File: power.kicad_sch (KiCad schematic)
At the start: 40 parts, among them T1 net-tie, U2 TPS546D24ARVFR

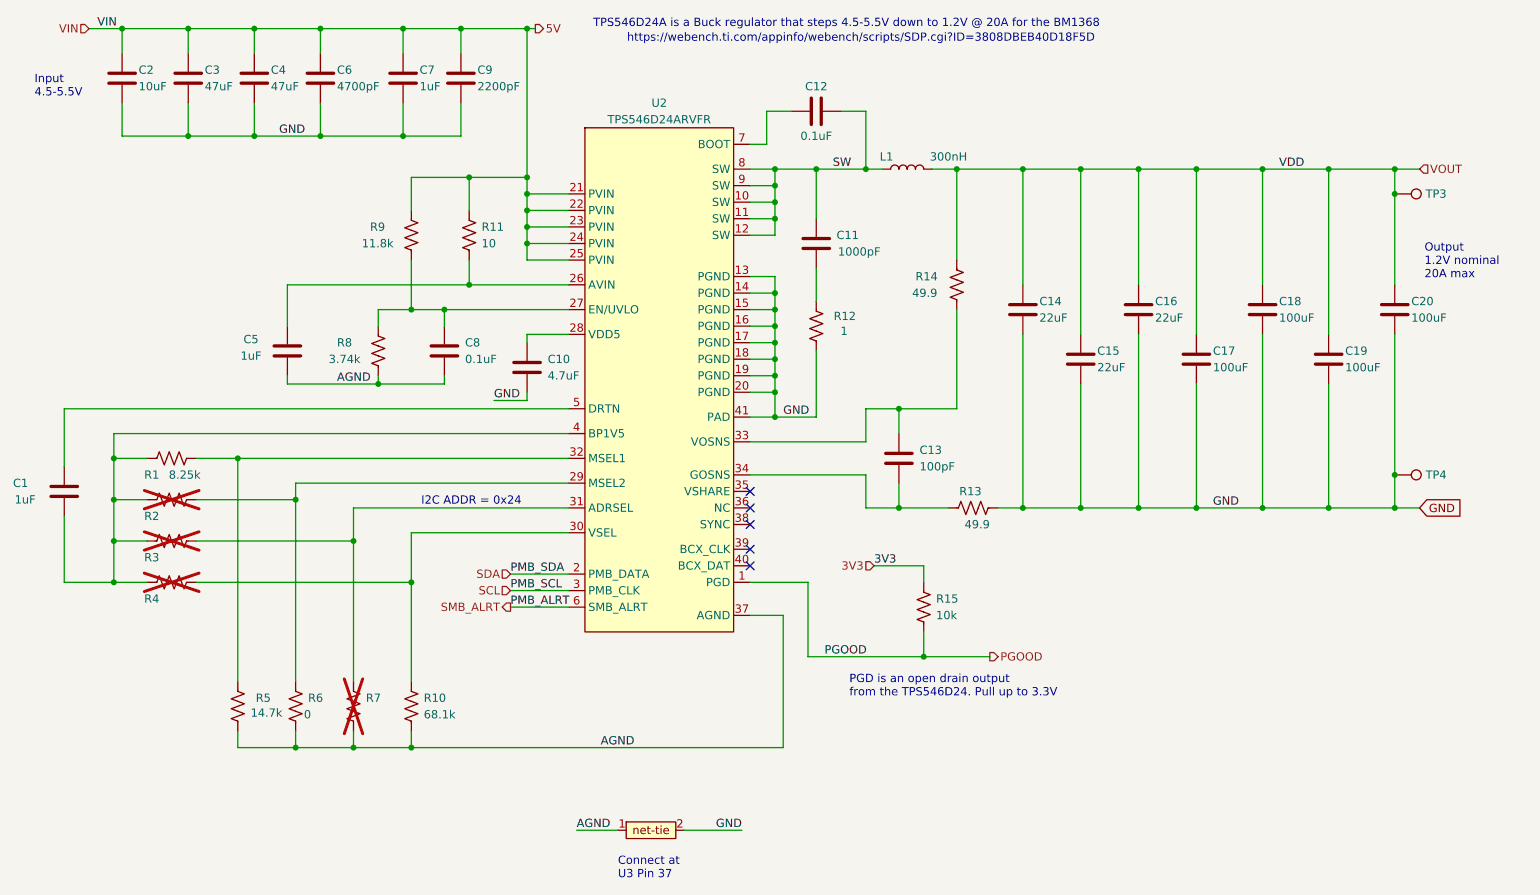
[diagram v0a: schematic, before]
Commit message: eco-603-impl: schematic ECO (E0-E6, R2-R3)
E0 #6/8bd74c8: R21 removed, U9.8 to 1V2, U9.9 direct GND.
E1 #47: U2 SYNC/BCX_CLK/BCX_DAT to AGND.
E2 #25 + R2: R30-R32 4k7 PMBus, R35 10k PGD pull-ups.
E3 #13/#16: R22/R23 100R to 10R.
E4 #11/#17: F1 5A series, D1 SMAJ5.0A, C60 bulk.
E5 #37 + R3: R33/R34 5k1 CC, D2/D5 USB ESD, D3/D4 I2C ESD.
R3: C61 47u + C62 100n PVIN/AVIN bulk.
Rev 601->603. ERC: 18->19 err (PVIN PWR flag side effect of F1,
same benign class); netlist-verified, geometry-audited.
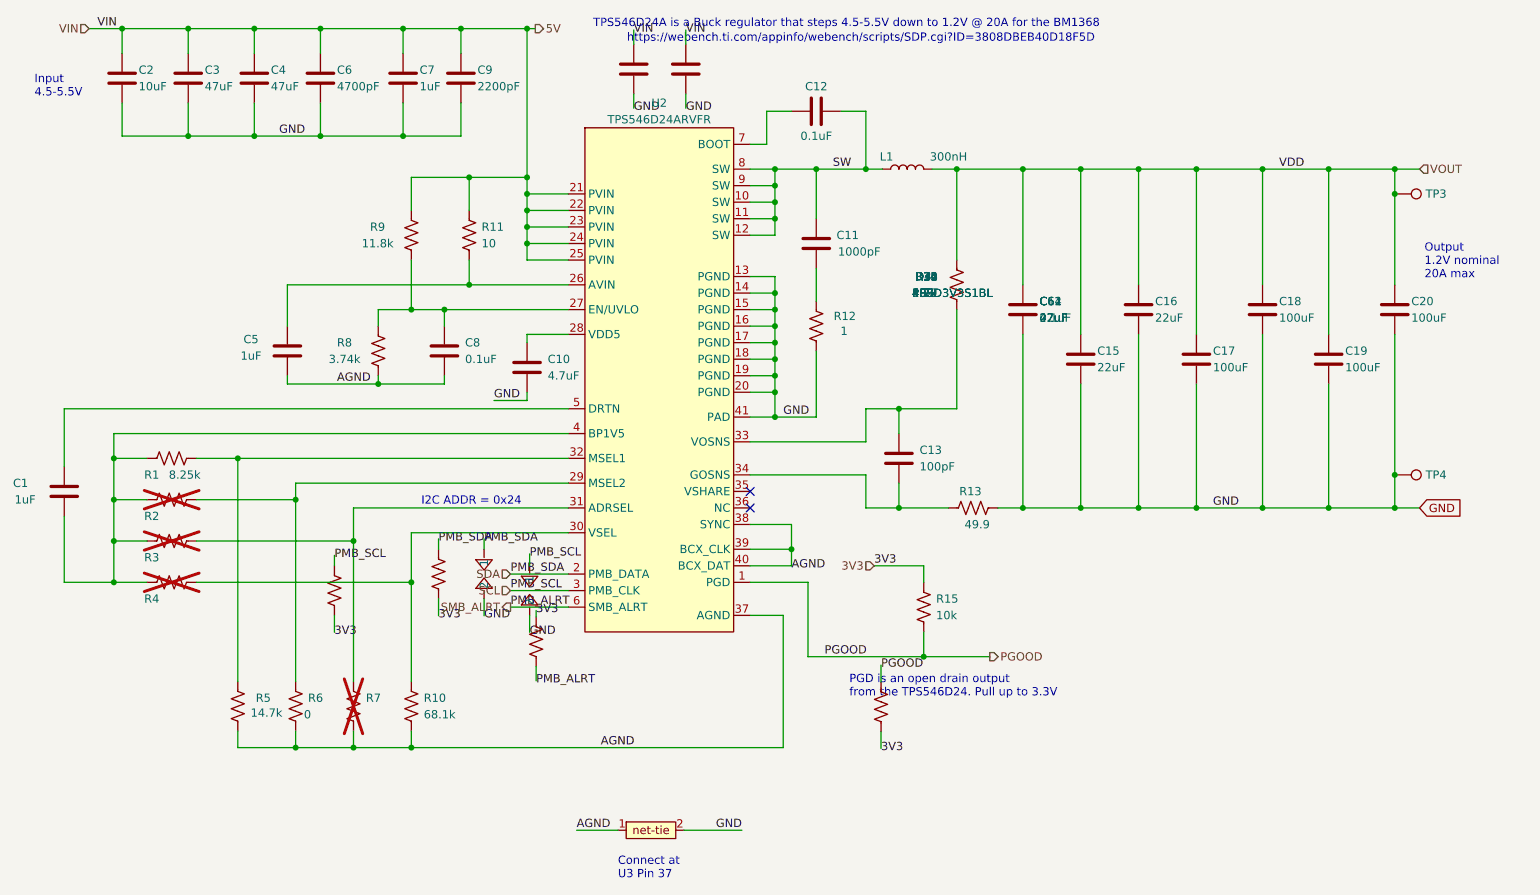
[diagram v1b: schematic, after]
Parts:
- added C61: 47uF, Capacitor_SMD:C_1206_3216Metric, symbol Device:C
- added C62: 0.1uF, Capacitor_SMD:C_0402_1005Metric, symbol Device:C
- added D3, D4: PESD3V3S1BL, Diode_SMD:D_SOD-323, symbol bitaxe:TVS_BIDIR
- added R30, R31, R32: 4.7k, Resistor_SMD:R_0402_1005Metric, symbol Device:R_US
- added R35: 10k, Resistor_SMD:R_0402_1005Metric, symbol Device:R_US
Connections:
- net 3V3: now also R30.2, R31.2, R32.1, R35.2
- net 5V: now also C61.1, C62.1
- net AGND: now also U2.38 (SYNC), U2.39 (BCX_CLK), U2.40 (BCX_DAT)
- net GND: now also C61.2, C62.2, D3.2, D4.2
- net PGOOD: now also R35.1
- net SCL: now also D4.1, R31.1
- net SDA: now also D3.1, R30.1
- net SMB_ALRT: now also R32.2
- no-connect marks 5 -> 2

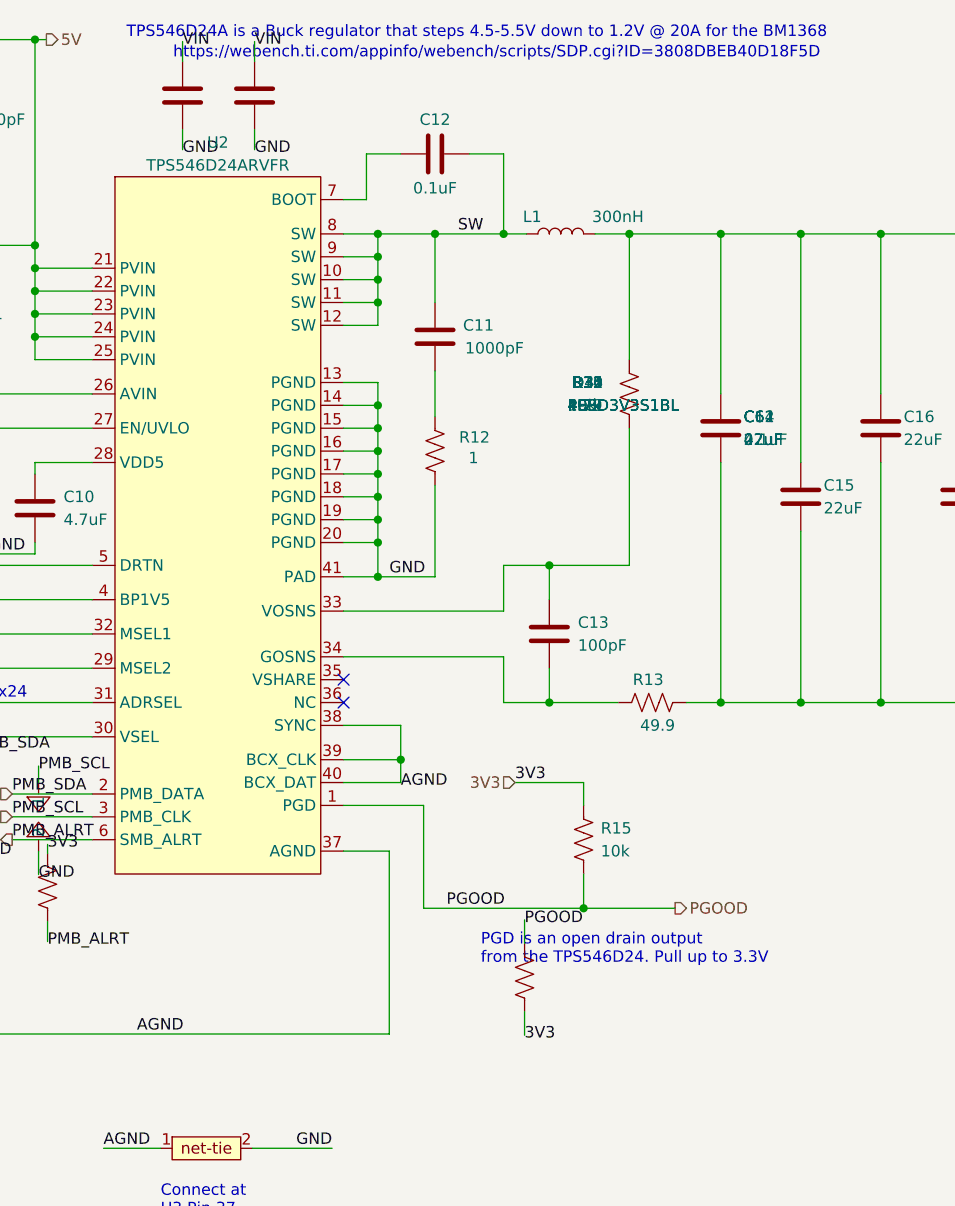
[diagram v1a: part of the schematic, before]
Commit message: eco-603-impl: PCB re-layout rev 603 (DRC 0 new) + manufacturing
PCB impl v7 (impl_pcb_603.py): herencia 602 + fixes E1-E6/R2-R3.
DRC con refill: 5 violaciones = base preexistente, 0 nuevas,
0 unconnected (drc_newZ.txt).
Regenera Gerbers/.drl/BOM/PDF esquematico desde esquematicos ECO
(sin R35/C61, D2->D2+D5, C60 1210, C62). iBOM html sin cambios
(no regenerable con kicad-cli; anotado).
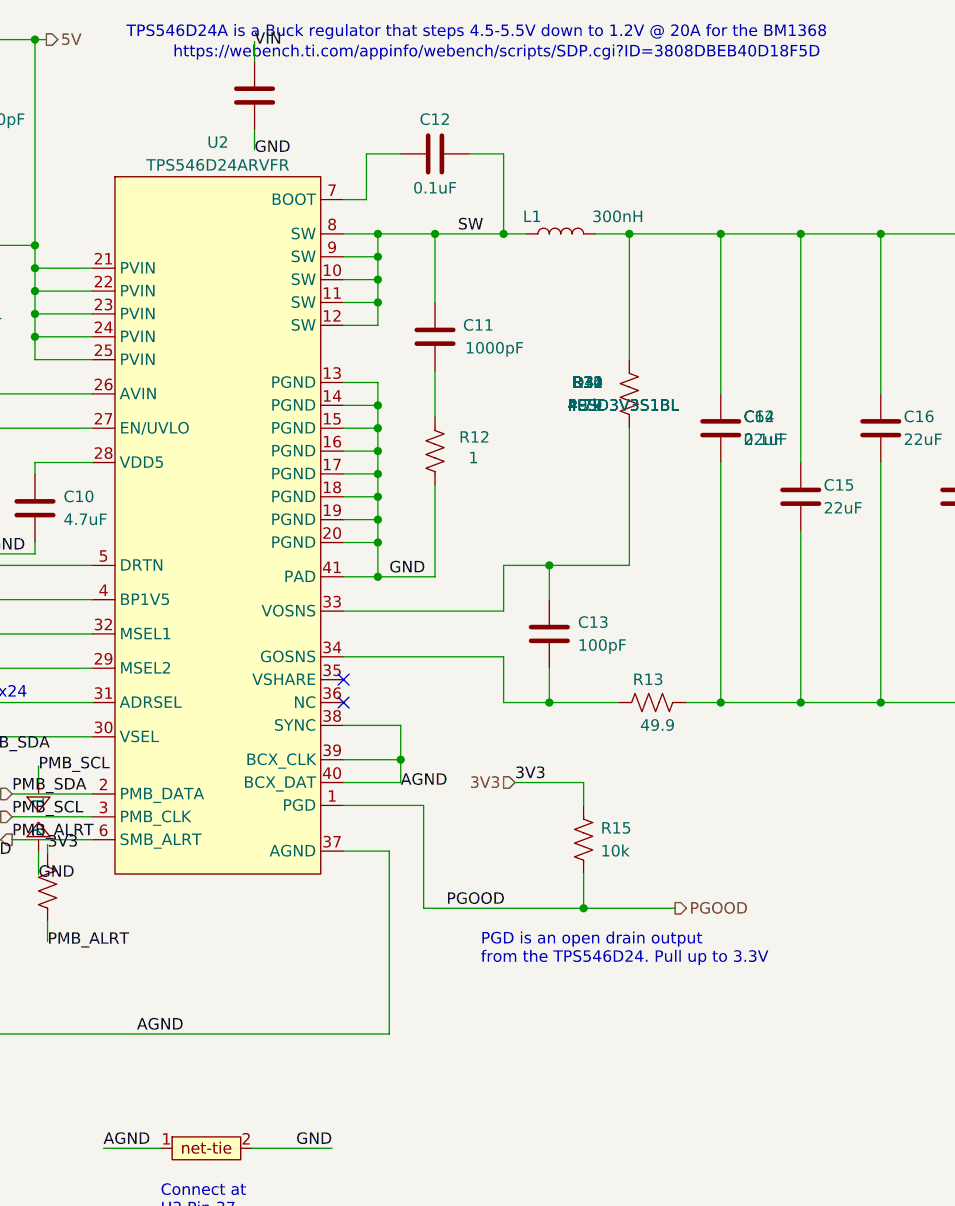
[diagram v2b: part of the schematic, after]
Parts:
- removed C61: 47uF, Capacitor_SMD:C_1206_3216Metric, symbol Device:C
- removed R35: 10k, Resistor_SMD:R_0402_1005Metric, symbol Device:R_US
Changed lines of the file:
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@@
-	(symbol
-		(lib_id "Device:R_US")
-		(at 156 122 0)
-		(unit 1)
-		(exclude_from_sim no)
-		(in_bom yes)
-		(on_board yes)
-		(dnp no)
-		(property "Reference" "R35"
-			(at 161.29 55.88 0)
-			(effects
-				(font
-					(size 1.27 1.27)
-				)
-				(justify left)
-			)
-		)
-		(property "Value" "10k"
-			(at 160.782 58.42 0)
-			(effects
-				(font
-					(size 1.27 1.27)
-				)
-				(justify left)
-			)
-		)
-		(property "Footprint" "Resistor_SMD:R_0402_1005Metric"
-			(at 168.656 57.404 90)
-			(effects
-				(font
-					(size 1.27 1.27)
-				)
-				(hide yes)
-			)
-		)
-		(property "Datasheet" "~"
-			(at 167.64 57.15 0)
-			(effects
-				(font
-					(size 1.27 1.27)
-				)
-				(hide yes)
-			)
-		)
-		(property "Description" ""
-			(at 167.64 57.15 0)
-			(effects
-				(font
-					(size 1.27 1.27)
-				)
-				(hide yes)
-			)
-		)
-		(property "DK" "311-10KJRCT-ND"
-			(at 167.64 57.15 0)
-			(effects
-				(font
-					(size 1.27 1.27)
-				)
-				(hide yes)
-			)
-		)
-		(property "PARTNO" "RC0402JR-0710KL"
-			(at 167.64 57.15 0)
-			(effects
-				(font
-					(size 1.27 1.27)
-				)
-				(hide yes)
-			)
-		)
-		(pin "1"
-		)
-		(pin "2"
-		)
-		(instances
-			(project "bitaxeGamma"
-				(path "/e63e39d7-6ac0-4ffd-8aa3-1841a4541b55/8ec0a9c6-2b78-44ef-a83d-9047d2828409"
-					(reference "R35")
-					(unit 1)
-				)
-			)
-		)
-	)
 	(symbol
 		(lib_id "Device:R_US")
@@
 	(symbol
 		(lib_id "Device:C")
-		(at 118 24 0)
-		(unit 1)
-		(exclude_from_sim no)
-		(in_bom yes)
-		(on_board yes)
-		(dnp no)
-		(property "Reference" "C61"
-			(at 180.34 59.69 0)
-			(effects
-				(font
-					(size 1.27 1.27)
-				)
-				(justify left)
-			)
-		)
-		(property "Value" "47uF"
-			(at 180.34 62.23 0)
-			(effects
-				(font
-					(size 1.27 1.27)
-				)
-				(justify left)
-			)
-		)
-		(property "Footprint" "Capacitor_SMD:C_1206_3216Metric"
-			(at 178.7652 64.77 0)
-			(effects
-				(font
-					(size 1.27 1.27)
-				)
-				(hide yes)
-			)
-		)
-		(property "Datasheet" ""
-			(at 177.8 60.96 0)
-			(effects
-				(font
-					(size 1.27 1.27)
-				)
-				(hide yes)
-			)
-		)
-		(property "Description" ""
-			(at 177.8 60.96 0)
-			(effects
-				(font
-					(size 1.27 1.27)
-				)
-				(hide yes)
-			)
-		)
-		(property "DK" "1276-3376-1-ND"
-			(at 177.8 60.96 0)
-			(effects
-				(font
-					(size 1.27 1.27)
-				)
-				(hide yes)
-			)
-		)
-		(property "PARTNO" "CL32A476KOJNNNE"
-			(at 177.8 60.96 0)
-			(effects
-				(font
-					(size 1.27 1.27)
-				)
-				(hide yes)
-			)
-		)
-		(pin "1"
-		)
-		(pin "2"
-		)
-		(instances
-			(project "bitaxeGamma"
-				(path "/e63e39d7-6ac0-4ffd-8aa3-1841a4541b55/8ec0a9c6-2b78-44ef-a83d-9047d2828409"
-					(reference "C61")
-					(unit 1)
-				)
-			)
-		)
-	)
-	(symbol
-		(lib_id "Device:C")
 		(at 126 24 0)
 		(unit 1)
@@
 	(wire
 		(pts
-			(xy 156 118.19) (xy 156 115.59)
-		)
-		(stroke
-			(width 0)
-			(type default)
-		)
-	)
-	(label "PGOOD"
-		(at 156 115.59 0)
-		(effects
-			(font
-				(size 1.27 1.27)
-			)
-		)
-	)
-	(wire
-		(pts
-			(xy 156 125.81) (xy 156 128.41)
-		)
-		(stroke
-			(width 0)
-			(type default)
-		)
-	)
-	(label "3V3"
-		(at 156 128.41 0)
-		(effects
-			(font
-				(size 1.27 1.27)
-			)
-		)
-	)
-	(wire
-		(pts
 			(xy 103 108.19) (xy 103 107.2)
 		)
@@
 		(effects
 			(font
-				(size 1.27 1.27)
-			)
-		)
-	)
-	(wire
-		(pts
-			(xy 118 20.19) (xy 118 17.99)
-		)
-		(stroke
-			(width 0)
-			(type default)
-		)
-	)
-	(label "VIN"
-		(at 118 17.99 0)
-		(effects
-			(font
-				(size 1.27 1.27)
-			)
-		)
-	)
-	(wire
-		(pts
-			(xy 118 27.81) (xy 118 30.01)
-		)
-		(stroke
-			(width 0)
-			(type default)
-		)
-	)
-	(label "GND"
-		(at 118 30.01 0)
-		(effects
-			(font
